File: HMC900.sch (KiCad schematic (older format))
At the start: 13 parts, among them U1 HMC900LP5E

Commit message: Corrected errors from single ended transition
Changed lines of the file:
@@
 F0 "sheet60F52DEE" 50
 F1 "Input_HMC900.sch" 50
-F2 "S+" I R 3000 4500 50
-F3 "S-" I R 3000 4650 50
+F2 "S+" I R 3000 4650 50
+F3 "S-" I R 3000 4500 50
 F4 "In" I L 2100 4550 50
 $EndSheet

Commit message: passage 0402 => 0603
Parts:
- C15, C16, C17, C18, C21, C22, C23, C25, C6, C7: footprint Capacitor_SMD:C_0402_1005Metric -> Capacitor_SMD:C_0603_1608Metric_Pad1.08x0.95mm_HandSolder
- R7, R8: footprint Resistor_SMD:R_0402_1005Metric -> Resistor_SMD:R_0603_1608Metric_Pad0.98x0.95mm_HandSolder
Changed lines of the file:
@@
 F 0 "C25" H 3375 3325 50  0000 R CNN
 F 1 "100n" H 3375 3500 50  0000 R CNN
-F 2 "Capacitor_SMD:C_0402_1005Metric" H 3438 3250 50  0001 C CNN
+F 2 "Capacitor_SMD:C_0603_1608Metric_Pad1.08x0.95mm_HandSolder" H 3438 3250 50  0001 C CNN
 F 3 "~" H 3400 3400 50  0001 C CNN
 	1    3400 3400
@@
 F 0 "C6" H 8615 3346 50  0000 L CNN
 F 1 "100n" H 8615 3255 50  0000 L CNN
-F 2 "Capacitor_SMD:C_0402_1005Metric" H 8538 3150 50  0001 C CNN
+F 2 "Capacitor_SMD:C_0603_1608Metric_Pad1.08x0.95mm_HandSolder" H 8538 3150 50  0001 C CNN
 F 3 "~" H 8500 3300 50  0001 C CNN
 	1    8500 3300
@@
 F 0 "C7" H 9015 3346 50  0000 L CNN
 F 1 "100p" H 9015 3255 50  0000 L CNN
-F 2 "Capacitor_SMD:C_0402_1005Metric" H 8938 3150 50  0001 C CNN
+F 2 "Capacitor_SMD:C_0603_1608Metric_Pad1.08x0.95mm_HandSolder" H 8938 3150 50  0001 C CNN
 F 3 "~" H 8900 3300 50  0001 C CNN
 	1    8900 3300
@@
 F 0 "C15" H 6115 1246 50  0000 L CNN
 F 1 "100n" H 6115 1155 50  0000 L CNN
-F 2 "Capacitor_SMD:C_0402_1005Metric" H 6038 1050 50  0001 C CNN
+F 2 "Capacitor_SMD:C_0603_1608Metric_Pad1.08x0.95mm_HandSolder" H 6038 1050 50  0001 C CNN
 F 3 "~" H 6000 1200 50  0001 C CNN
 	1    6000 1200
@@
 F 0 "C22" H 3725 3325 50  0000 R CNN
 F 1 "100p" H 3725 3500 50  0000 R CNN
-F 2 "Capacitor_SMD:C_0402_1005Metric" H 3788 3250 50  0001 C CNN
+F 2 "Capacitor_SMD:C_0603_1608Metric_Pad1.08x0.95mm_HandSolder" H 3788 3250 50  0001 C CNN
 F 3 "~" H 3750 3400 50  0001 C CNN
 	1    3750 3400
@@
 F 0 "R8" H 7270 3896 50  0000 L CNN
 F 1 "51" H 7270 3805 50  0000 L CNN
-F 2 "Resistor_SMD:R_0402_1005Metric" V 7130 3850 50  0001 C CNN
+F 2 "Resistor_SMD:R_0603_1608Metric_Pad0.98x0.95mm_HandSolder" V 7130 3850 50  0001 C CNN
 F 3 "~" H 7200 3850 50  0001 C CNN
 	1    7200 3850
@@
 F 0 "R7" V 7550 3600 50  0000 C CNN
 F 1 "0" V 7450 3600 50  0000 C CNN
-F 2 "Resistor_SMD:R_0402_1005Metric" V 7380 3600 50  0001 C CNN
+F 2 "Resistor_SMD:R_0603_1608Metric_Pad0.98x0.95mm_HandSolder" V 7380 3600 50  0001 C CNN
 F 3 "~" H 7450 3600 50  0001 C CNN
 	1    7450 3600
@@
 F 0 "C16" H 6065 5546 50  0000 L CNN
 F 1 "100n" H 6065 5455 50  0000 L CNN
-F 2 "Capacitor_SMD:C_0402_1005Metric" H 5988 5350 50  0001 C CNN
+F 2 "Capacitor_SMD:C_0603_1608Metric_Pad1.08x0.95mm_HandSolder" H 5988 5350 50  0001 C CNN
 F 3 "~" H 5950 5500 50  0001 C CNN
 	1    5950 5500
@@
 F 0 "C21" H 4725 1800 50  0000 R CNN
 F 1 "100n" H 4725 1975 50  0000 R CNN
-F 2 "Capacitor_SMD:C_0402_1005Metric" H 4788 1725 50  0001 C CNN
+F 2 "Capacitor_SMD:C_0603_1608Metric_Pad1.08x0.95mm_HandSolder" H 4788 1725 50  0001 C CNN
 F 3 "~" H 4750 1875 50  0001 C CNN
 	1    4750 1875
@@
 F 0 "C17" H 5125 1800 50  0000 R CNN
 F 1 "100p" H 5125 1975 50  0000 R CNN
-F 2 "Capacitor_SMD:C_0402_1005Metric" H 5188 1725 50  0001 C CNN
+F 2 "Capacitor_SMD:C_0603_1608Metric_Pad1.08x0.95mm_HandSolder" H 5188 1725 50  0001 C CNN
 F 3 "~" H 5150 1875 50  0001 C CNN
 	1    5150 1875
@@
 F 0 "C23" H 4975 4775 50  0000 R CNN
 F 1 "100n" H 4975 4950 50  0000 R CNN
-F 2 "Capacitor_SMD:C_0402_1005Metric" H 5038 4700 50  0001 C CNN
+F 2 "Capacitor_SMD:C_0603_1608Metric_Pad1.08x0.95mm_HandSolder" H 5038 4700 50  0001 C CNN
 F 3 "~" H 5000 4850 50  0001 C CNN
 	1    5000 4850
@@
 F 0 "C18" H 5375 4775 50  0000 R CNN
 F 1 "100p" H 5375 4950 50  0000 R CNN
-F 2 "Capacitor_SMD:C_0402_1005Metric" H 5438 4700 50  0001 C CNN
+F 2 "Capacitor_SMD:C_0603_1608Metric_Pad1.08x0.95mm_HandSolder" H 5438 4700 50  0001 C CNN
 F 3 "~" H 5400 4850 50  0001 C CNN
 	1    5400 4850

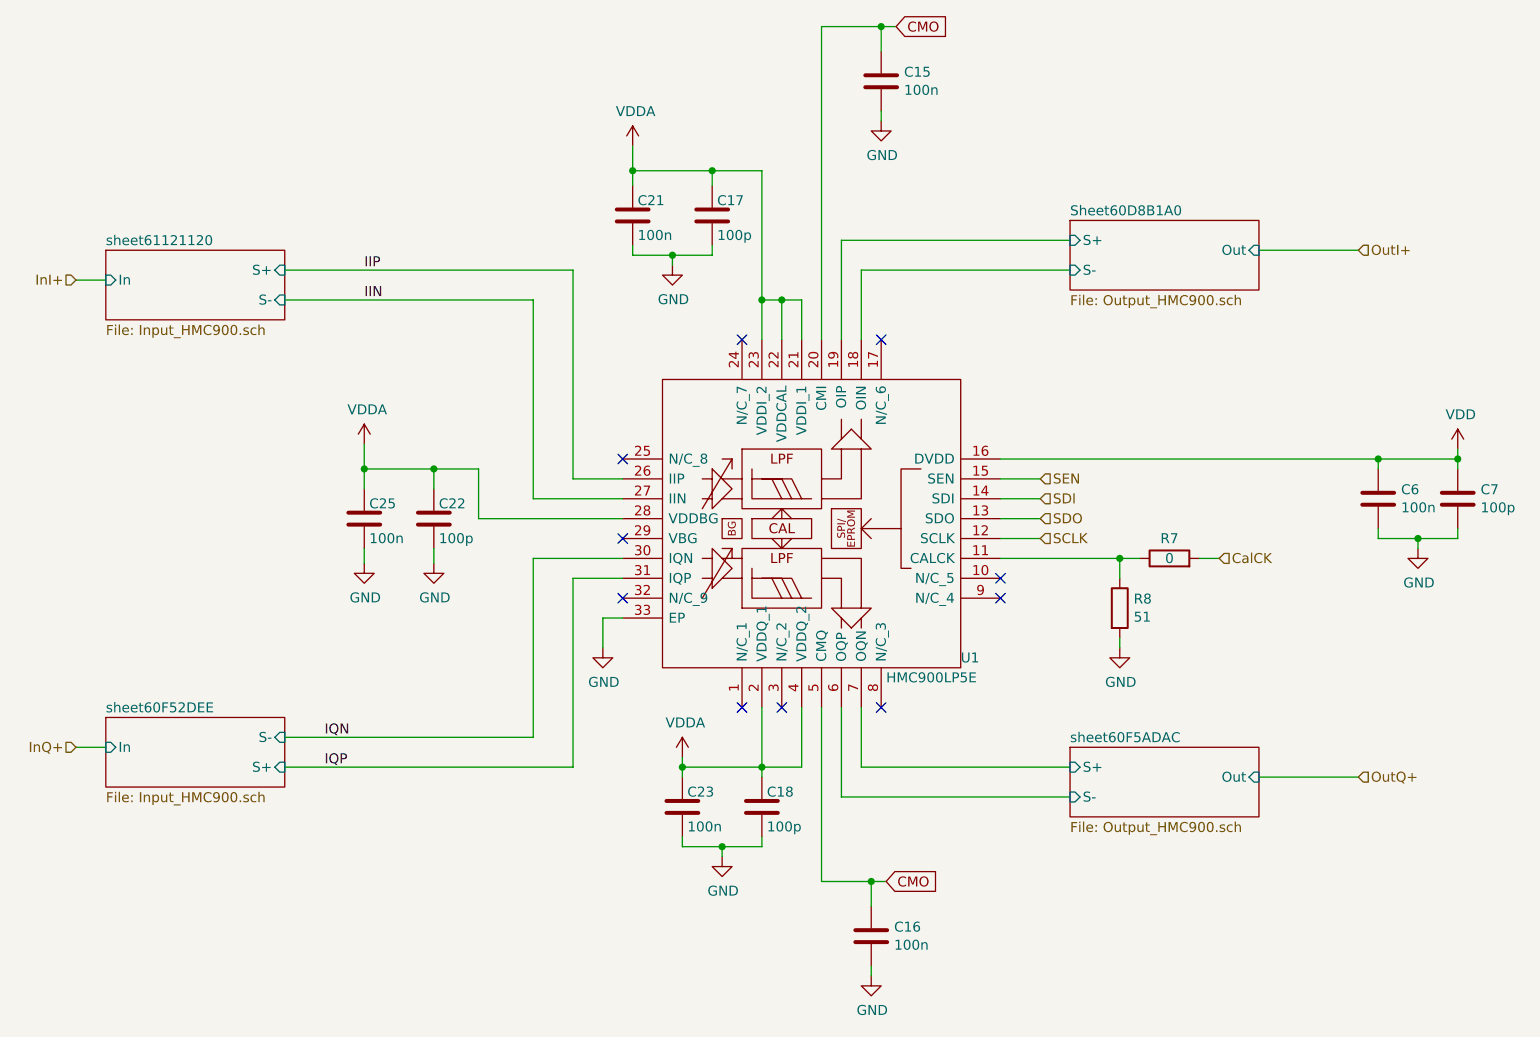
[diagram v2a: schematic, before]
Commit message: Made the 2 DS1085 signals merge before the filter Looped the filter's 1st output to the now liberated 2nd input to double the filtration Added a protection diode before the filter
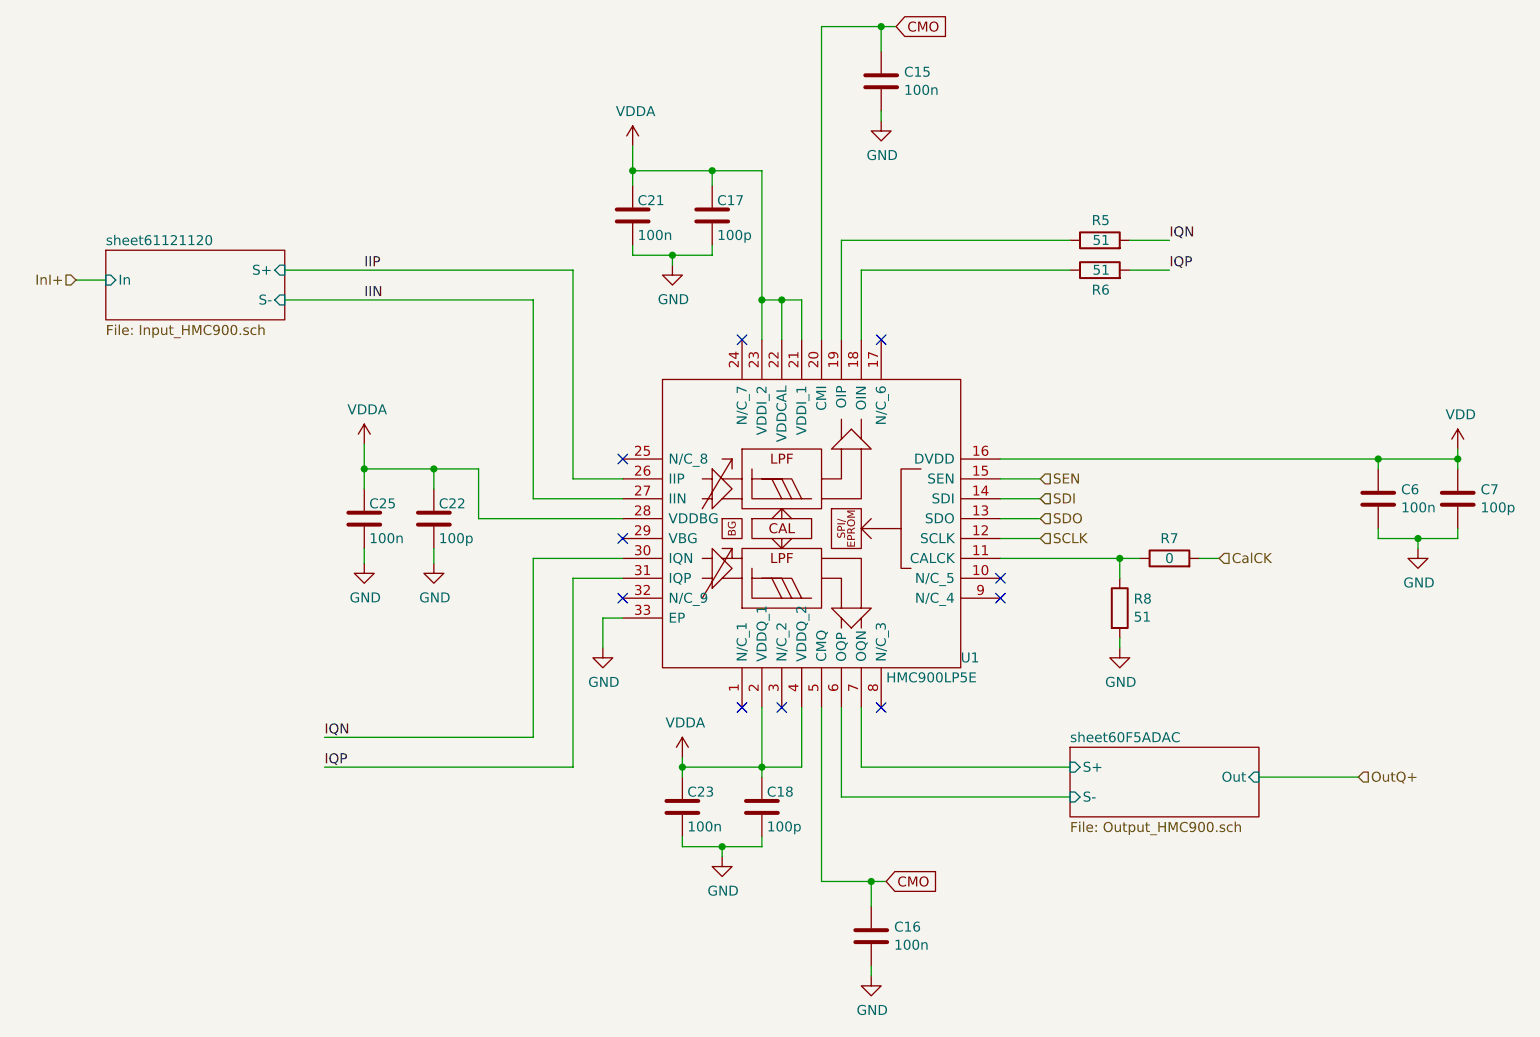
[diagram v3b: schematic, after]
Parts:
- added R5, R6: 51, Resistor_SMD:R_0603_1608Metric_Pad0.98x0.95mm_HandSolder, symbol Device:R
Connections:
- net IQN: now also R5.2
- net IQP: now also R6.2
- net Sheet60D8B1A0/S+: no longer names the net of U1.19 (OIP)
- net Sheet60D8B1A0/S+: now also R5.1
- net Sheet60D8B1A0/S-: no longer names the net of U1.18 (OIN)
- net Sheet60D8B1A0/S-: now also R6.1
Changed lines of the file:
@@
 $Descr A4 11693 8268
 encoding utf-8
-Sheet 2 7
+Sheet 2 5
 Title ""
 Date ""
@@
 Comment4 ""
 $EndDescr
-$Sheet
-S 6950 1900 950  350
-U 60D8B1A1
-F0 "Sheet60D8B1A0" 50
-F1 "Output_HMC900.sch" 50
-F2 "S+" I L 6950 2000 50
-F3 "S-" I L 6950 2150 50
-F4 "Out" I R 7900 2050 50
-$EndSheet
 $Comp
 L Device:C C25
@@
 $EndSheet
 Wire Wire Line
-	3000 4500 4250 4500
+	3200 4500 4250 4500
 Wire Wire Line
 	4250 3600 4250 4500
 Wire Wire Line
-	3000 4650 4450 4650
+	3200 4650 4450 4650
 Wire Wire Line
 	4450 3700 4450 4650
-Wire Wire Line
-	2100 4550 1950 4550
-Text HLabel 1950 4550 0    50   Input ~ 0
-InQ+
 Wire Wire Line
 	5400 1650 5400 2300
@@
 Wire Wire Line
 	5800 4800 6950 4800
-Wire Wire Line
-	7900 2050 8400 2050
-Text HLabel 8400 2050 2    50   Input ~ 0
-OutI+
 Wire Wire Line
 	7900 4700 8400 4700
@@
 	2100 2200 1950 2200
 $Sheet
-S 2100 4400 900  350
-U 60F52DEE
-F0 "sheet60F52DEE" 50
-F1 "Input_HMC900.sch" 50
-F2 "S+" I R 3000 4650 50
-F3 "S-" I R 3000 4500 50
-F4 "In" I L 2100 4550 50
-$EndSheet
-$Sheet
 S 6950 4550 950  350
 U 60F5ADAC
@@
 F4 "Out" I R 7900 4700 50
 $EndSheet
+Wire Wire Line
+	7250 2000 7450 2000
+Wire Wire Line
+	7250 2150 7450 2150
+Text Label 7450 2000 0    50   ~ 0
+IQN
+Text Label 7450 2150 0    50   ~ 0
+IQP
+$Comp
+L Device:R R5
+U 1 1 61B49135
+P 7100 2000
+F 0 "R5" V 7200 1950 50  0000 L CNN
+F 1 "51" V 7100 1950 50  0000 L CNN
+F 2 "Resistor_SMD:R_0603_1608Metric_Pad0.98x0.95mm_HandSolder" V 7030 2000 50  0001 C CNN
+F 3 "~" H 7100 2000 50  0001 C CNN
+	1    7100 2000
+	0    -1   -1   0
+$EndComp
+$Comp
+L Device:R R6
+U 1 1 61B5A7B5
+P 7100 2150
+F 0 "R6" V 7000 2100 50  0000 L CNN
+F 1 "51" V 7100 2100 50  0000 L CNN
+F 2 "Resistor_SMD:R_0603_1608Metric_Pad0.98x0.95mm_HandSolder" V 7030 2150 50  0001 C CNN
+F 3 "~" H 7100 2150 50  0001 C CNN
+	1    7100 2150
+	0    -1   -1   0
+$EndComp
 $EndSCHEMATC
